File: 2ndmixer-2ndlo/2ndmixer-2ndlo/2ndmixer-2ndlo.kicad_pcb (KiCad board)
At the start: 2 copper layers, 72.4 x 49.5 mm, 59 parts, among them J201 Coax Solder Point, J202 Conn_01x02, J203 Coax Solder Point, Q201 2N5179, Q202 2N5179, T201 Bifilar_Transformer, U201 MAV-11, U202 TUF-1H+, Y201 100MHz

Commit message: partial 2nd lo fixes
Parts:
- TP203: value Q-Emit1 -> Q-Coll1
- TP204: value Q-Coll1 -> Q-Emit1
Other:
- board text added: "Spectrum Analyzer 2nd Mixer 2nd Local Osc. Rev 2"
- board text removed: "Spectrum Analyzer 2nd Mixer 2nd Local Osc. Rev 1"
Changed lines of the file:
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@@
     (title "Spectrum Analyzer: Second Mixer - Second Local Oscillator")
     (date "2023-03-11")
-    (rev "1")
+    (rev "1.1")
     (company "Andy McCann KA3KAF Doug McCann KA3KAG")
-    (comment 2 "Wes Hayward W7ZOI")
-    (comment 3 "Original Design By:")
+    (comment 1 "Original Design By: Wes Hayward W7ZOI")
+    (comment 2 "V0: 9/1/22")
+    (comment 3 "V1: 3/23/23 (redesign closer to Kanga)")
+    (comment 4 "V2: 11/19/23 (new C206, Fix silk TP203/204")
   )
   (layers
@@
     (property "Sim.Device" "SPICE")
     (property "Sim.Enable" "0")
-    (property "Sim.Params" "Q-Coll1")
+    (property "Sim.Params" "Q-Emit1")
     (property "Sim.Pins" "1=1")
     (property "ki_description" "test point (alternative probe-style design)")
@@
         (effects (font (size 0.75 0.75) (thickness 0.15)))
     )
-    (fp_text value "Q-Coll1" (at 0 1.55) (layer "F.Fab")
+    (fp_text value "Q-Emit1" (at 0 1.55) (layer "F.Fab")
         (effects (font (size 1 1) (thickness 0.15)))
     )
-    (fp_text user "Q-Coll1" (at 3.5052 0.9652 unlocked) (layer "F.SilkS")
+    (fp_text user "Q-Emit1" (at 3.5052 0.9652 unlocked) (layer "F.SilkS")
         (effects (font (size 0.75 0.75) (thickness 0.15)))
     )
@@
     (property "Sim.Device" "SPICE")
     (property "Sim.Enable" "0")
-    (property "Sim.Params" "Q-Emit1")
+    (property "Sim.Params" "Q-Coll11")
     (property "Sim.Pins" "1=1")
     (property "ki_description" "test point (alternative probe-style design)")
@@
         (effects (font (size 0.75 0.75) (thickness 0.15)))
     )
-    (fp_text value "Q-Emit1" (at 0 1.55) (layer "F.Fab")
+    (fp_text value "Q-Coll1" (at 0 1.55) (layer "F.Fab")
         (effects (font (size 1 1) (thickness 0.15)))
     )
-    (fp_text user "Q-Emit1" (at 3.556 0.8636 unlocked) (layer "F.SilkS")
+    (fp_text user "Q-Coll1" (at 3.556 0.8636 unlocked) (layer "F.SilkS")
         (effects (font (size 0.75 0.75) (thickness 0.15)))
     )
@@
     (effects (font (size 1 1) (thickness 0.25)))
   )
-  (gr_text "Spectrum Analyzer\n2nd Mixer 2nd Local Osc. Rev 1" (at 187.198 76.8096) (layer "F.SilkS")
+  (gr_text "Spectrum Analyzer\n2nd Mixer 2nd Local Osc. Rev 2" (at 187.198 76.8096) (layer "F.SilkS")
     (effects (font (size 1 1) (thickness 0.25)))
   )

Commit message: latest 2ndlo
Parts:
- added C215: .01u, Capacitor_THT:C_Disc_D5.0mm_W2.5mm_P5.00mm, F.Cu at (175.4, 118.4)
- C206: footprint spectrum_analyzer:GKG60015 -> spectrum_analyzer:BFC280831659
- moved R215 12.2 mm to (178.7, 86.8)
- moved C206 6.25 mm to (170.6, 77.8)
- moved C213 4.33 mm to (178.6, 79.6)
- moved R204 3.77 mm to (161.6, 79.3)
- moved TP202 3.54 mm to (158.9, 77.5)
- moved C208 2.69 mm to (169.3, 91.9)
- moved T201 1.92 mm to (182.3, 84.4)
- moved R213 1.85 mm to (201.1, 85.6)
- moved R217 1.14 mm to (182.7, 118.4)
- moved C214 0.38 mm to (197.7, 118.4)
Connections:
- C204 pad 1: Net-(C204-Pad1) -> Net-(C206-S)
- C206 pad 1: Net-(C204-Pad1) -> GND
- C206 pad 2: GND -> Net-(C206-S)
- C207 pad 1: Net-(C204-Pad1) -> Net-(C206-S)
- L201 pad 2: Net-(C204-Pad1) -> Net-(C206-S)
- L203 pad 2: GND -> Net-(U201-RF_Out)
- Q201 pad 3: Net-(C204-Pad1) -> Net-(C206-S)
- TP203 pad 1: Net-(C204-Pad1) -> Net-(C206-S)
- TP208 pad 1: GND -> Net-(U201-RF_Out)
- U201 pad 3: GND -> Net-(U201-RF_Out)
- U202 pad 4: GND -> Net-(U202-LO)
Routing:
- net GND: track 222.8 -> 0.00 mm
- net Net-(C206-S): track 0.00 -> 68.5 mm
- net Net-(C204-Pad1): track 55.3 -> 0.00 mm
- net Net-(U201-RF_Out): track 0.00 -> 34.4 mm
- net Net-(C212-Pad2): track 46.6 -> 25.7 mm
- net Net-(U201-RF_In): track 51.9 -> 36.3 mm
- net Net-(J203-In): track 30.6 -> 45.9 mm
- net Net-(L202-Pad2): track 35.3 -> 48.7 mm
- net Net-(J201-In): track 46.9 -> 59.5 mm
- net /+15: track 83.3 -> 95.4 mm
- net Net-(U202-LO): track 0.00 -> 11.6 mm
- net Net-(U202-IF): track 28.2 -> 23.2 mm
- net Net-(C203-Pad1): track 35.5 -> 40.0 mm
- net Net-(C213-Pad2): track 10.6 -> 14.6 mm
- net Net-(Q202-Pad3): track 47.0 -> 50.6 mm
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
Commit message: updates to 2nd lo
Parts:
- moved TP210 21.0 mm to (193.1, 104.1)
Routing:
- net GND: track 0.00 -> 226.0 mm
- net Net-(C206-S): track 68.5 -> 53.5 mm
- net Net-(J203-In): track 45.9 -> 32.1 mm
- net Net-(L202-Pad2): track 48.7 -> 35.3 mm
- net Net-(U202-IF): track 23.2 -> 28.1 mm
- net Net-(Q202-Pad3): track 50.6 -> 45.9 mm
- net Net-(J201-In): track 59.5 -> 55.0 mm
- net Net-(U201-RF_Out): track 34.4 -> 30.1 mm
- net Net-(C201-Pad1): track 40.6 -> 37.3 mm
- net Net-(C209-Pad1): track 23.0 -> 19.9 mm
- net Net-(C212-Pad2): track 25.7 -> 23.3 mm
- net Net-(C203-Pad1): track 40.0 -> 38.1 mm
- net /+15: track 95.4 -> 93.5 mm
- net Net-(U201-RF_In): track 36.3 -> 37.4 mm
- net Net-(C213-Pad2): track 14.6 -> 14.1 mm

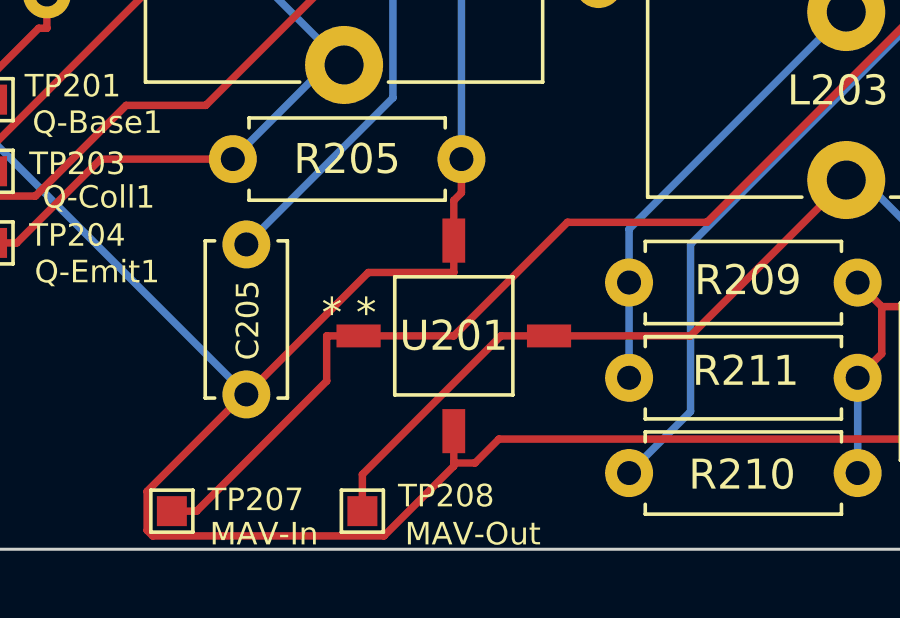
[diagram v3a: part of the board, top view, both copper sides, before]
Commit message: further change to 2nd LO schematic and board
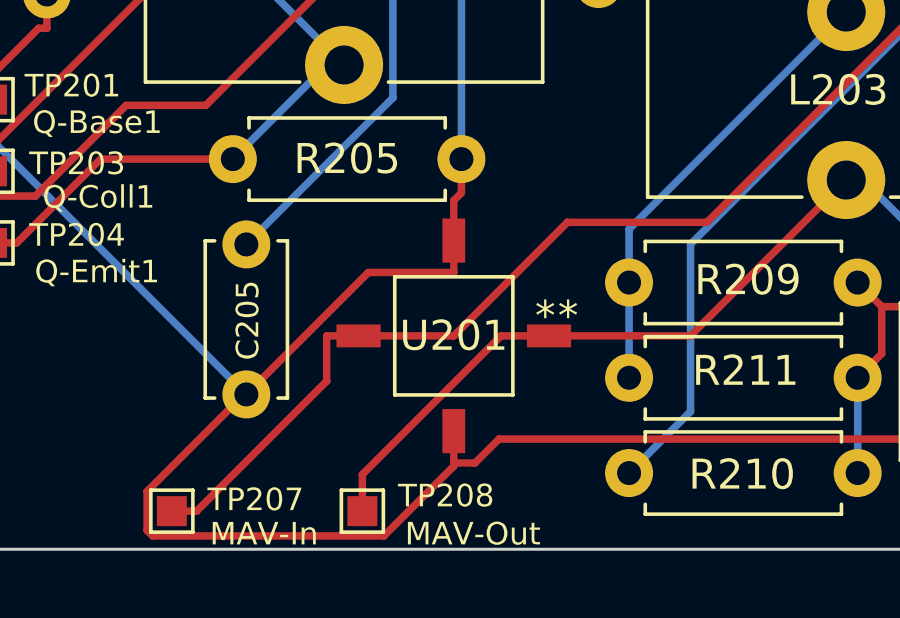
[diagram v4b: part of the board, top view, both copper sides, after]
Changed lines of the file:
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@@
     (title "Spectrum Analyzer: Second Mixer - Second Local Oscillator")
     (date "2023-03-11")
-    (rev "1.1")
+    (rev "2")
     (company "Andy McCann KA3KAF Doug McCann KA3KAG")
     (comment 1 "Original Design By: Wes Hayward W7ZOI")
     (comment 2 "V0: 9/1/22")
     (comment 3 "V1: 3/23/23 (redesign closer to Kanga)")
-    (comment 4 "V2: 11/19/23 (new C206, Fix silk TP203/204")
+    (comment 4 "V2: 11/29/23 (new C206, Fix silk TP203/204, fixed silk mav-11)")
   )
   (layers
@@
         (effects (font (size 1 1) (thickness 0.15)))
     )
-    (fp_text user "*" (at -4.064 -0.762) (layer "F.SilkS")
-        (effects (font (size 1 1) (thickness 0.15)))
-    )
-    (fp_text user "*" (at -2.921 -0.762) (layer "F.SilkS")
+    (fp_text user "*" (at 3.81 -0.6604) (layer "F.SilkS")
+        (effects (font (size 1 1) (thickness 0.15)))
+    )
+    (fp_text user "*" (at 3.048 -0.6604) (layer "F.SilkS")
         (effects (font (size 1 1) (thickness 0.15)))
     )
     (fp_text user "0.058in/1.473mm" (at 7.4295 -3.175) (layer "Cmts.User")
-        (effects (font (size 1 1) (thickness 0.15)))
-    )
-    (fp_text user "0.25in/6.35mm" (at 0 7.874) (layer "Cmts.User")
         (effects (font (size 1 1) (thickness 0.15)))
     )
@@
         (effects (font (size 1 1) (thickness 0.15)))
     )
+    (fp_text user "0in/0mm" (at 6.604 0) (layer "Cmts.User")
+        (effects (font (size 1 1) (thickness 0.15)))
+    )
     (fp_text user "0.03in/0.762mm" (at 0 -6.604) (layer "Cmts.User")
         (effects (font (size 1 1) (thickness 0.15)))
     )
-    (fp_text user "0in/0mm" (at 6.604 0) (layer "Cmts.User")
-        (effects (font (size 1 1) (thickness 0.15)))
-    )
+    (fp_text user "0.25in/6.35mm" (at 0 7.874) (layer "Cmts.User")
+        (effects (font (size 1 1) (thickness 0.15)))
+    )

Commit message: Match to Kanga layout
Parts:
- J203: renamed from J201; value Coax Solder Point -> 110 MHz In
- J204: renamed from J203; value Coax Solder Point -> 2nd IF Out
- renumbered C203 to C202, C204 to C203, C205 to C204, C207 to C205, C208 to C206, C211 to C208, C215 to C211, C213 to C212, C214 to C213, C212 to C214, C206 to C299, J202 to J201, R203 to R201, R201 to R203, R205 to R204, R204 to R205, R210 to R209, R209 to R210, R216 to R215, R217 to R216, R215 to R217
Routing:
- net Net-(J204-In): track 32.1 -> 25.4 mm
- net GND: track 226.0 -> 221.8 mm
- net Net-(Q202-Pad3): track 45.9 -> 48.8 mm
- net Net-(C214-Pad2): track 23.3 -> 24.7 mm
- net Net-(Q202-Pad1): track 35.1 -> 36.1 mm
- net /+15: track 93.5 -> 92.7 mm
- net Net-(U201-RF_In): track 37.4 -> 38.3 mm

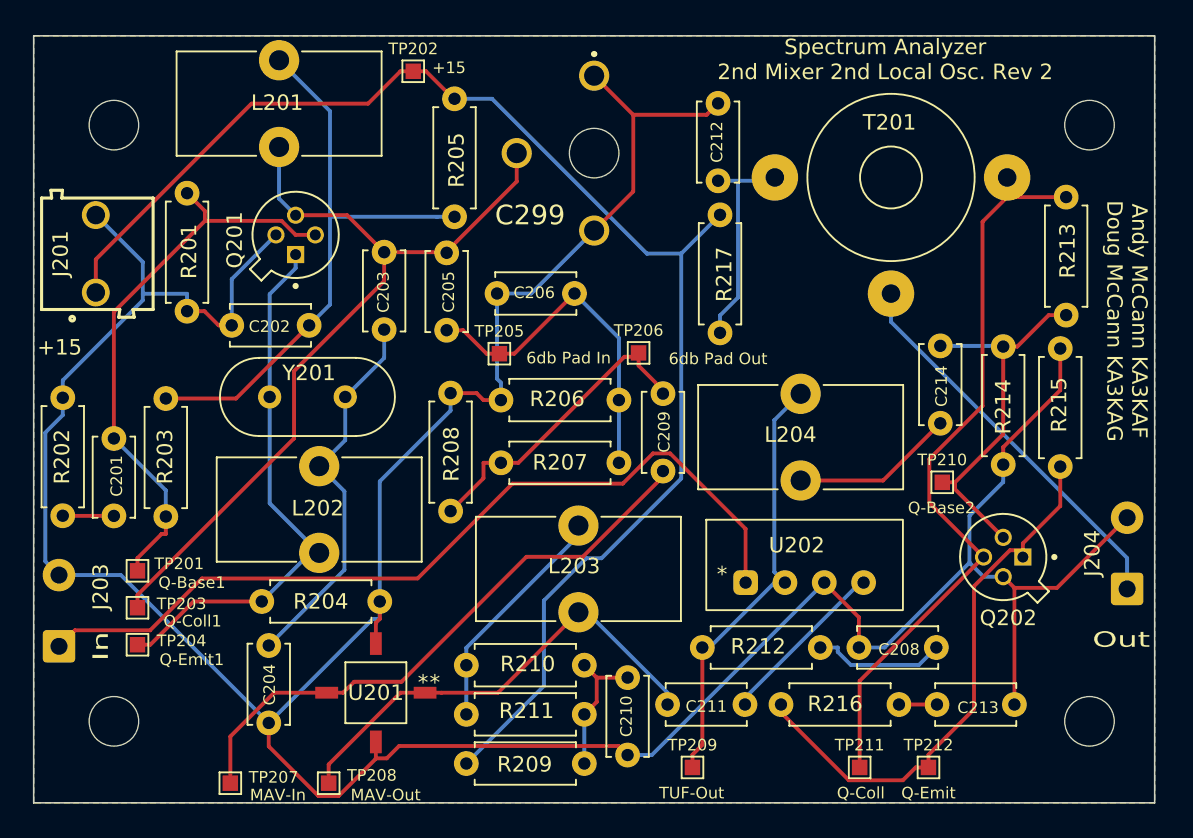
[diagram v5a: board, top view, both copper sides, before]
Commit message: 2ndmixer-2ndlo.kicad_sch change to ADE-1H
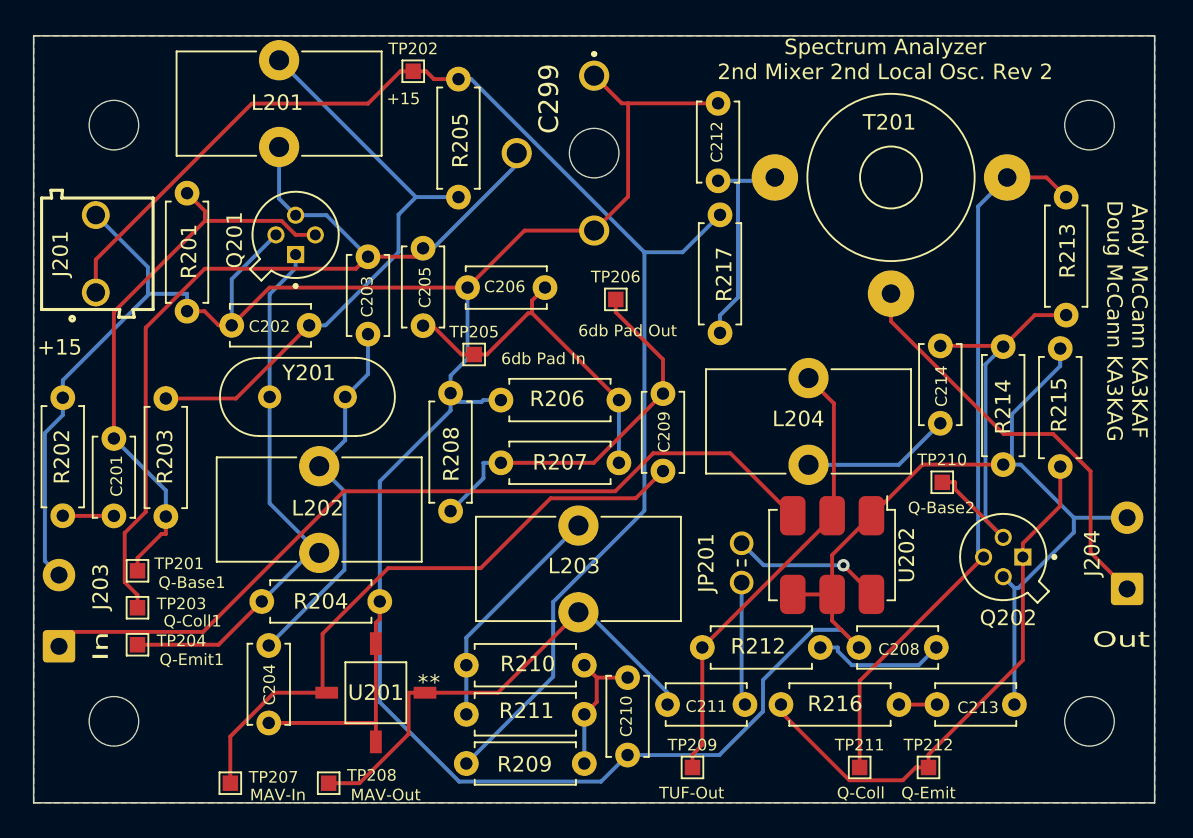
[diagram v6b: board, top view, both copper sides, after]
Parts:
- added JP201: 5025, spectrum_analyzer:KEYSTONE_5025, F.Cu at (180.1, 109.3)
- TP209: value TUF-Out -> ADE-Out
- U202: value TUF-1H+ -> ADE-1HW+; footprint spectrum_analyzer:TUF-1H -> spectrum_analyzer:Mini-Circuits_CD636_H4.11mm
- moved U202 5.86 mm to (186.0, 108.8), turned to -90 degrees
- moved TP206 3.76 mm to (172.0, 92.3)
- moved C206 1.94 mm to (167.4, 91.5)
- moved TP205 1.63 mm to (162.9, 95.8)
- moved C205 1.55 mm to (159.6, 89.0)
- moved R205 1.30 mm to (161.8, 78.0)
- moved L204 1.14 mm to (184.5, 97.3)
- moved C203 1.08 mm to (156.0, 89.5)
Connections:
- C211 pad 2: Net-(U202-LO) -> Net-(C211-Pad2)
- U202 pad 1: Net-(J203-In) -> GND
- U202 pad 3: GND -> Net-(J203-In)
- U202 pad 4: Net-(U202-LO) -> GND
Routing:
- net Net-(C211-Pad2): track 0.00 -> 7.96 mm
- net GND: track 221.8 -> 228.6 mm
- net Net-(C299-S): track 53.5 -> 58.7 mm
- net Net-(C209-Pad1): track 20.1 -> 24.8 mm
- net Net-(C214-Pad2): track 24.7 -> 27.9 mm
- net Net-(U201-RF_In): track 38.3 -> 40.6 mm
- net Net-(Q202-Pad3): track 48.8 -> 46.7 mm
- net Net-(J204-In): track 25.4 -> 27.3 mm
- net /+15: track 92.7 -> 91.1 mm
- net Net-(U202-IF): track 28.1 -> 29.6 mm
- net Net-(U202-LO): track 11.2 -> 9.79 mm, vias 0 -> 1
- net Net-(Q202-Pad1): track 36.1 -> 35.1 mm
- net Net-(C214-Pad1): track 10.5 -> 9.62 mm
- net Net-(U201-RF_Out): track 30.1 -> 30.9 mm
- net Net-(J203-In): track 55.0 -> 54.2 mm
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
